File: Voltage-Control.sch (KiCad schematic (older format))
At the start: 6 parts, among them U201 MCP6002

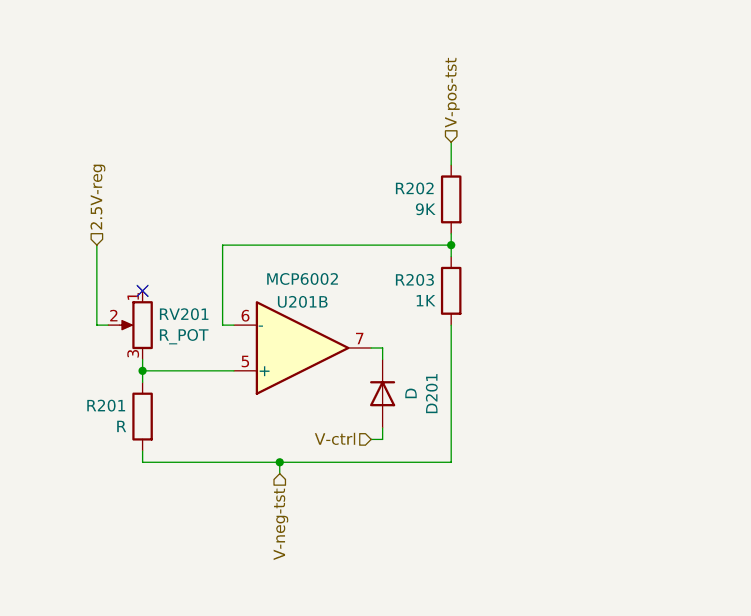
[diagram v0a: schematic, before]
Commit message: PCB completed with Op-Amp mounted horizontally
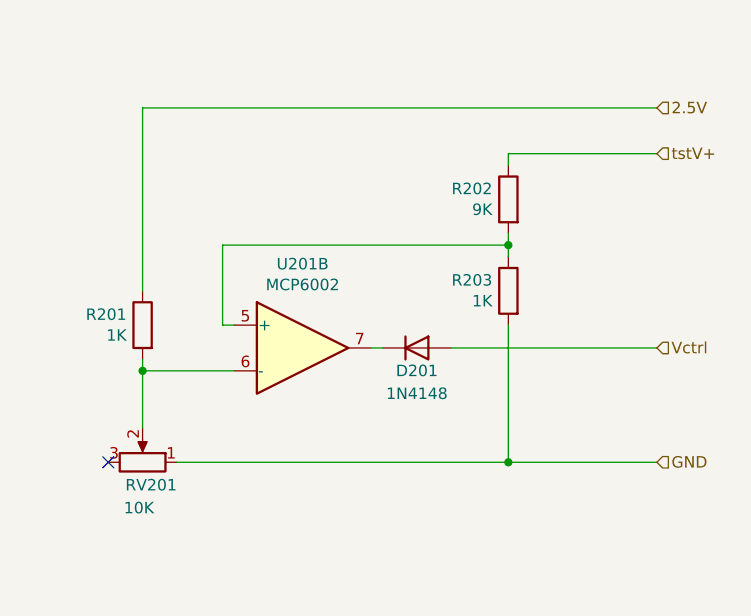
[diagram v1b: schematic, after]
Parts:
- D201: value D -> 1N4148; footprint Diode_SMD:D_SMA_Handsoldering -> Diode_SMD:D_SOD-123
- R201: value R -> 1K
- RV201: value R_POT -> 10K; footprint Potentiometer_THT:Potentiometer_Bourns_3266Y_Vertical -> f:POT_TTElect_P160KN; MPN (none) -> P160KN-0QD15B10K
- U201: footprint Package_SO:SOIC-8_3.9x4.9mm_P1.27mm -> (none)
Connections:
- net at R202.2, R203.1: now also U201.5 (+); no longer U201.6 (-)
- net GND: now reaches RV201.1
- net GND: now also R203.2
- net 2.5V-reg: no longer names the net of RV201.2
- net 2.5V-reg: now also R201.2, U201.6 (-)
- net V-ctrl renamed Vctrl
- removed net V-neg-tst: R201.2, R203.2
- net V-pos-tst renamed tstV+
- new net 2.5V: R201.1
- now unconnected: RV201.3
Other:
- moved on the sheet: D201, R201, R202, R203, RV201
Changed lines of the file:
@@
 L Device:D D?
 U 1 1 6016A51E
-P 5800 3450
+P 5950 3250
 AR Path="/6016A51E" Ref="D?"  Part="1"
 AR Path="/601B79A0/6016A51E" Ref="D201"  Part="1"
-F 0 "D201" H 5800 3667 50  0000 C CNN
-F 1 "D" H 5800 3576 50  0000 C CNN
-F 2 "Diode_SMD:D_SMA_Handsoldering" H 5800 3450 50  0001 C CNN
-F 3 "~" H 5800 3450 50  0001 C CNN
-	1    5800 3450
-	0    1    1    0
+F 0 "D201" H 5950 3150 50  0000 C CNN
+F 1 "1N4148" H 5950 3050 50  0000 C CNN
+F 2 "Diode_SMD:D_SOD-123" H 5950 3250 50  0001 C CNN
+F 3 "~" H 5950 3250 50  0001 C CNN
+	1    5950 3250
+	1    0    0    -1
 $EndComp
 $Comp
 L Device:R_POT RV?
 U 1 1 6016A525
-P 4750 3150
+P 4750 3750
 AR Path="/6016A525" Ref="RV?"  Part="1"
 AR Path="/601B79A0/6016A525" Ref="RV201"  Part="1"
-F 0 "RV201" H 4681 3196 50  0000 R CNN
-F 1 "R_POT" H 4681 3105 50  0000 R CNN
-F 2 "Potentiometer_THT:Potentiometer_Bourns_3266Y_Vertical" H 4750 3150 50  0001 C CNN
+F 0 "RV201" V 4650 3900 50  0000 R CNN
+F 1 "10K" V 4550 3800 50  0000 R CNN
+F 2 "f:POT_TTElect_P160KN" H 4750 3750 50  0001 C CNN
+F 3 "https://www.ttelectronics.com/TTElectronics/media/ProductFiles/Potentiometers/Datasheets/P160.pdf" H 4750 3750 50  0001 C CNN
+F 4 "P160KN-0QD15B10K" H 4750 3750 50  0001 C CNN "MPN"
+	1    4750 3750
+	0    1    -1   0
+$EndComp
+$Comp
+L Device:R R?
+U 1 1 6016A52B
+P 4750 3150
+AR Path="/6016A52B" Ref="R?"  Part="1"
+AR Path="/601B79A0/6016A52B" Ref="R201"  Part="1"
+F 0 "R201" H 4820 3196 50  0000 L CNN
+F 1 "1K" H 4820 3105 50  0000 L CNN
+F 2 "Resistor_SMD:R_0805_2012Metric_Pad1.20x1.40mm_HandSolder" V 4680 3150 50  0001 C CNN
 F 3 "~" H 4750 3150 50  0001 C CNN
 	1    4750 3150
 	-1   0    0    -1
 $EndComp
-$Comp
-L Device:R R?
-U 1 1 6016A52B
-P 4750 3550
-AR Path="/6016A52B" Ref="R?"  Part="1"
-AR Path="/601B79A0/6016A52B" Ref="R201"  Part="1"
-F 0 "R201" H 4820 3596 50  0000 L CNN
-F 1 "R" H 4820 3505 50  0000 L CNN
-F 2 "Resistor_SMD:R_0805_2012Metric_Pad1.20x1.40mm_HandSolder" V 4680 3550 50  0001 C CNN
-F 3 "~" H 4750 3550 50  0001 C CNN
-	1    4750 3550
-	-1   0    0    -1
-$EndComp
-Wire Wire Line
-	4750 3700 4750 3750
 Wire Wire Line
 	5100 3150 5100 2800
@@
 L Device:R R?
 U 1 1 6016A53B
-P 6100 3000
+P 6350 3000
 AR Path="/6016A53B" Ref="R?"  Part="1"
 AR Path="/601B79A0/6016A53B" Ref="R203"  Part="1"
-F 0 "R203" H 6170 3046 50  0000 L CNN
-F 1 "1K" H 6170 2955 50  0000 L CNN
-F 2 "Resistor_SMD:R_0805_2012Metric_Pad1.20x1.40mm_HandSolder" V 6030 3000 50  0001 C CNN
-F 3 "~" H 6100 3000 50  0001 C CNN
-	1    6100 3000
+F 0 "R203" H 6420 3046 50  0000 L CNN
+F 1 "1K" H 6420 2955 50  0000 L CNN
+F 2 "Resistor_SMD:R_0805_2012Metric_Pad1.20x1.40mm_HandSolder" V 6280 3000 50  0001 C CNN
+F 3 "~" H 6350 3000 50  0001 C CNN
+	1    6350 3000
 	-1   0    0    -1
 $EndComp
@@
 L Device:R R?
 U 1 1 6016A541
-P 6100 2600
+P 6350 2600
 AR Path="/6016A541" Ref="R?"  Part="1"
 AR Path="/601B79A0/6016A541" Ref="R202"  Part="1"
-F 0 "R202" H 6170 2646 50  0000 L CNN
-F 1 "9K" H 6170 2555 50  0000 L CNN
-F 2 "Resistor_SMD:R_0805_2012Metric_Pad1.20x1.40mm_HandSolder" V 6030 2600 50  0001 C CNN
-F 3 "~" H 6100 2600 50  0001 C CNN
-	1    6100 2600
+F 0 "R202" H 6420 2646 50  0000 L CNN
+F 1 "9K" H 6420 2555 50  0000 L CNN
+F 2 "Resistor_SMD:R_0805_2012Metric_Pad1.20x1.40mm_HandSolder" V 6280 2600 50  0001 C CNN
+F 3 "~" H 6350 2600 50  0001 C CNN
+	1    6350 2600
 	-1   0    0    -1
 $EndComp
 Wire Wire Line
-	6100 2750 6100 2800
+	6350 2750 6350 2800
 Wire Wire Line
-	6100 2800 5100 2800
-Connection ~ 6100 2800
+	6350 2800 5100 2800
+Connection ~ 6350 2800
 Wire Wire Line
-	6100 2800 6100 2850
-Text HLabel 6100 2350 1    50   Input ~ 0
-V-pos-tst
+	6350 2800 6350 2850
+Text HLabel 7000 2400 2    50   Input ~ 0
+tstV+
 Wire Wire Line
-	4600 3150 4550 3150
-Wire Wire Line
-	4550 3150 4550 2800
-Wire Wire Line
-	5750 3250 5800 3250
-Wire Wire Line
-	5800 3250 5800 3300
-Wire Wire Line
-	4750 3750 5350 3750
-Wire Wire Line
-	6100 3750 6100 3150
-Wire Wire Line
-	5350 3800 5350 3750
-Connection ~ 5350 3750
-Wire Wire Line
-	5350 3750 6100 3750
-NoConn ~ 4750 3000
-Text HLabel 5750 3650 0    50   Input ~ 0
-V-ctrl
-Wire Wire Line
-	5750 3650 5800 3650
-Wire Wire Line
-	5800 3650 5800 3600
-Wire Wire Line
-	6100 2350 6100 2450
-Text HLabel 4550 2800 1    50   Input ~ 0
-2.5V-reg
-Text HLabel 5350 3800 3    50   Input ~ 0
-V-neg-tst
-Wire Wire Line
-	4750 3300 4750 3350
-$Comp
-L Amplifier_Operational:MCP6002-xSN U?
-U 2 1 6016A517
-P 5450 3250
-AR Path="/6016A517" Ref="U?"  Part="2"
-AR Path="/601B79A0/6016A517" Ref="U201"  Part="2"
-F 0 "U201" H 5450 3050 50  0000 C CNN
-F 1 "MCP6002" H 5450 2950 50  0000 C CNN
-F 2 "Package_SO:SOIC-8_3.9x4.9mm_P1.27mm" H 5450 3250 50  0001 C CNN
-F 3 "http://ww1.microchip.com/downloads/en/DeviceDoc/21733j.pdf" H 5450 3250 50  0001 C CNN
-	2    5450 3250
-	1    0    0    1
-$EndComp
+	6350 3750 6350 3150
+NoConn ~ 4600 3750
+Text HLabel 7000 3250 2    50   Input ~ 0
+Vctrl
+Text HLabel 7000 2200 2    50   Input ~ 0
+2.5V
+Text HLabel 7000 3750 2    50   Input ~ 0
+GND
 Wire Wire Line
 	5100 3150 5150 3150
@@
 Connection ~ 4750 3350
 Wire Wire Line
-	4750 3350 4750 3400
+	4750 3350 4750 3600
+Wire Wire Line
+	4750 3300 4750 3350
+Wire Wire Line
+	6350 2400 6350 2450
+Wire Wire Line
+	6350 2400 7000 2400
+Connection ~ 6350 3750
+Wire Wire Line
+	6350 3750 7000 3750
+Wire Wire Line
+	4900 3750 6350 3750
+Wire Wire Line
+	4750 2200 4750 3000
+Wire Wire Line
+	4750 2200 7000 2200
+Wire Wire Line
+	5750 3250 5800 3250
+Wire Wire Line
+	6100 3250 7000 3250
+$Comp
+L Amplifier_Operational:MCP6002-xSN U201
+U 2 1 60396245
+P 5450 3250
+F 0 "U201" H 5450 3617 50  0000 C CNN
+F 1 "MCP6002" H 5450 3526 50  0000 C CNN
+F 2 "" H 5450 3250 50  0001 C CNN
+F 3 "http://ww1.microchip.com/downloads/en/DeviceDoc/21733j.pdf" H 5450 3250 50  0001 C CNN
+	2    5450 3250
+	1    0    0    -1
+$EndComp
 $EndSCHEMATC

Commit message: Revision A as sent to OSHPark with some MPN updates due to availability
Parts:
- R201, R202, R203: footprint Resistor_SMD:R_0805_2012Metric_Pad1.20x1.40mm_HandSolder -> Resistor_SMD:R_0603_1608Metric_Pad0.98x0.95mm_HandSolder
- U201: footprint (none) -> Package_SO:SOIC-8_3.9x4.9mm_P1.27mm; MPN (none) -> MCP6002T-I/SN
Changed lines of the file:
@@
 F 0 "R201" H 4820 3196 50  0000 L CNN
 F 1 "1K" H 4820 3105 50  0000 L CNN
-F 2 "Resistor_SMD:R_0805_2012Metric_Pad1.20x1.40mm_HandSolder" V 4680 3150 50  0001 C CNN
+F 2 "Resistor_SMD:R_0603_1608Metric_Pad0.98x0.95mm_HandSolder" V 4680 3150 50  0001 C CNN
 F 3 "~" H 4750 3150 50  0001 C CNN
 	1    4750 3150
@@
 F 0 "R203" H 6420 3046 50  0000 L CNN
 F 1 "1K" H 6420 2955 50  0000 L CNN
-F 2 "Resistor_SMD:R_0805_2012Metric_Pad1.20x1.40mm_HandSolder" V 6280 3000 50  0001 C CNN
+F 2 "Resistor_SMD:R_0603_1608Metric_Pad0.98x0.95mm_HandSolder" V 6280 3000 50  0001 C CNN
 F 3 "~" H 6350 3000 50  0001 C CNN
 	1    6350 3000
@@
 F 0 "R202" H 6420 2646 50  0000 L CNN
 F 1 "9K" H 6420 2555 50  0000 L CNN
-F 2 "Resistor_SMD:R_0805_2012Metric_Pad1.20x1.40mm_HandSolder" V 6280 2600 50  0001 C CNN
+F 2 "Resistor_SMD:R_0603_1608Metric_Pad0.98x0.95mm_HandSolder" V 6280 2600 50  0001 C CNN
 F 3 "~" H 6350 2600 50  0001 C CNN
 	1    6350 2600
@@
 F 0 "U201" H 5450 3617 50  0000 C CNN
 F 1 "MCP6002" H 5450 3526 50  0000 C CNN
-F 2 "" H 5450 3250 50  0001 C CNN
+F 2 "Package_SO:SOIC-8_3.9x4.9mm_P1.27mm" H 5450 3250 50  0001 C CNN
 F 3 "http://ww1.microchip.com/downloads/en/DeviceDoc/21733j.pdf" H 5450 3250 50  0001 C CNN
+F 4 "MCP6002T-I/SN" H 5450 3250 50  0001 C CNN "MPN"
 	2    5450 3250
 	1    0    0    -1

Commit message: Revision 1 release
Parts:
- R202: value 9K -> 9.1K
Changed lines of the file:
@@
 AR Path="/601B79A0/6016A541" Ref="R202"  Part="1"
 F 0 "R202" H 6420 2646 50  0000 L CNN
-F 1 "9K" H 6420 2555 50  0000 L CNN
+F 1 "9.1K" H 6420 2555 50  0000 L CNN
 F 2 "Resistor_SMD:R_0603_1608Metric_Pad0.98x0.95mm_HandSolder" V 6280 2600 50  0001 C CNN
 F 3 "~" H 6350 2600 50  0001 C CNN

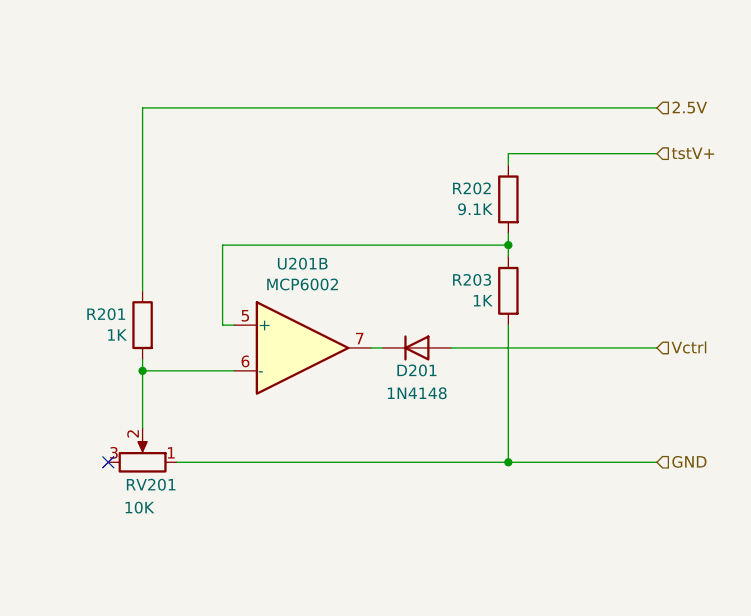
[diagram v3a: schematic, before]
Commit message: Fixed reversed Op-Amp for voltage limiting and potentiometer connections to allow for full range of the potentiometer.
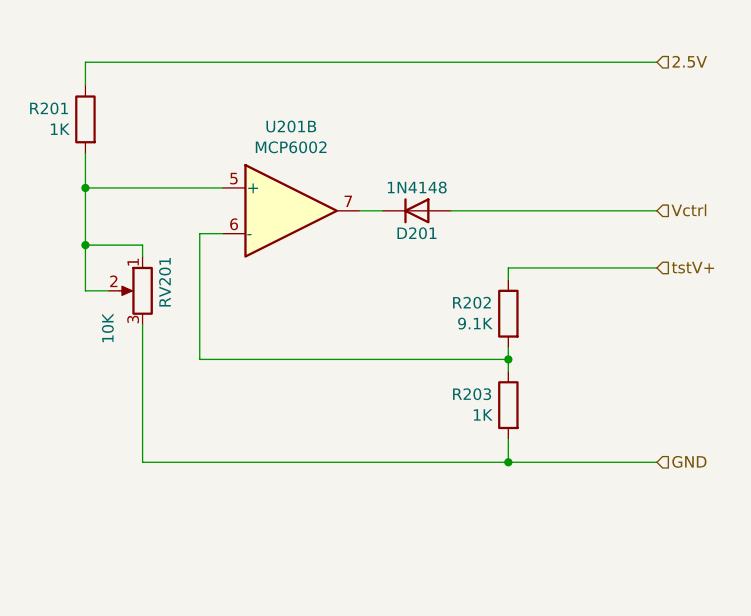
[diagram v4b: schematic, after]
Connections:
- net GND: now also RV201.3; no longer RV201.1
- net at R201.2, RV201.2: now also RV201.1, U201.5 (+); no longer U201.6 (-)
- net at R202.2, R203.1: now also U201.6 (-); no longer U201.5 (+)
- no-connect marks 1 -> 0
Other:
- moved on the sheet: D201, R201, R202, R203, RV201, U201B
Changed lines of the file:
@@
 L Device:D D?
 U 1 1 6016A51E
-P 5950 3250
+P 5950 2650
 AR Path="/6016A51E" Ref="D?"  Part="1"
 AR Path="/601B79A0/6016A51E" Ref="D201"  Part="1"
-F 0 "D201" H 5950 3150 50  0000 C CNN
-F 1 "1N4148" H 5950 3050 50  0000 C CNN
-F 2 "Diode_SMD:D_SOD-123" H 5950 3250 50  0001 C CNN
-F 3 "~" H 5950 3250 50  0001 C CNN
-	1    5950 3250
+F 0 "D201" H 5950 2550 50  0000 C CNN
+F 1 "1N4148" H 5950 2750 50  0000 C CNN
+F 2 "Diode_SMD:D_SOD-123" H 5950 2650 50  0001 C CNN
+F 3 "~" H 5950 2650 50  0001 C CNN
+	1    5950 2650
 	1    0    0    -1
 $EndComp
@@
 L Device:R_POT RV?
 U 1 1 6016A525
-P 4750 3750
+P 4750 3000
 AR Path="/6016A525" Ref="RV?"  Part="1"
 AR Path="/601B79A0/6016A525" Ref="RV201"  Part="1"
-F 0 "RV201" V 4650 3900 50  0000 R CNN
-F 1 "10K" V 4550 3800 50  0000 R CNN
-F 2 "f:POT_TTElect_P160KN" H 4750 3750 50  0001 C CNN
-F 3 "https://www.ttelectronics.com/TTElectronics/media/ProductFiles/Potentiometers/Datasheets/P160.pdf" H 4750 3750 50  0001 C CNN
-F 4 "P160KN-0QD15B10K" H 4750 3750 50  0001 C CNN "MPN"
-	1    4750 3750
-	0    1    -1   0
+F 0 "RV201" V 4650 3150 50  0000 R CNN
+F 1 "10K" V 4900 2900 50  0000 R CNN
+F 2 "f:POT_TTElect_P160KN" H 4750 3000 50  0001 C CNN
+F 3 "https://www.ttelectronics.com/TTElectronics/media/ProductFiles/Potentiometers/Datasheets/P160.pdf" H 4750 3000 50  0001 C CNN
+F 4 "P160KN-0QD15B10K" H 4750 3000 50  0001 C CNN "MPN"
+	1    4750 3000
+	-1   0    0    -1
 $EndComp
 $Comp
 L Device:R R?
 U 1 1 6016A52B
-P 4750 3150
+P 4500 2250
 AR Path="/6016A52B" Ref="R?"  Part="1"
 AR Path="/601B79A0/6016A52B" Ref="R201"  Part="1"
-F 0 "R201" H 4820 3196 50  0000 L CNN
-F 1 "1K" H 4820 3105 50  0000 L CNN
-F 2 "Resistor_SMD:R_0603_1608Metric_Pad0.98x0.95mm_HandSolder" V 4680 3150 50  0001 C CNN
-F 3 "~" H 4750 3150 50  0001 C CNN
-	1    4750 3150
+F 0 "R201" H 4570 2296 50  0000 L CNN
+F 1 "1K" H 4570 2205 50  0000 L CNN
+F 2 "Resistor_SMD:R_0603_1608Metric_Pad0.98x0.95mm_HandSolder" V 4430 2250 50  0001 C CNN
+F 3 "~" H 4500 2250 50  0001 C CNN
+	1    4500 2250
 	-1   0    0    -1
 $EndComp
-Wire Wire Line
-	5100 3150 5100 2800
 $Comp
 L Device:R R?
 U 1 1 6016A53B
-P 6350 3000
+P 6350 3500
 AR Path="/6016A53B" Ref="R?"  Part="1"
 AR Path="/601B79A0/6016A53B" Ref="R203"  Part="1"
-F 0 "R203" H 6420 3046 50  0000 L CNN
-F 1 "1K" H 6420 2955 50  0000 L CNN
-F 2 "Resistor_SMD:R_0603_1608Metric_Pad0.98x0.95mm_HandSolder" V 6280 3000 50  0001 C CNN
-F 3 "~" H 6350 3000 50  0001 C CNN
-	1    6350 3000
+F 0 "R203" H 6420 3546 50  0000 L CNN
+F 1 "1K" H 6420 3455 50  0000 L CNN
+F 2 "Resistor_SMD:R_0603_1608Metric_Pad0.98x0.95mm_HandSolder" V 6280 3500 50  0001 C CNN
+F 3 "~" H 6350 3500 50  0001 C CNN
+	1    6350 3500
 	-1   0    0    -1
 $EndComp
@@
 L Device:R R?
 U 1 1 6016A541
-P 6350 2600
+P 6350 3100
 AR Path="/6016A541" Ref="R?"  Part="1"
 AR Path="/601B79A0/6016A541" Ref="R202"  Part="1"
-F 0 "R202" H 6420 2646 50  0000 L CNN
-F 1 "9.1K" H 6420 2555 50  0000 L CNN
-F 2 "Resistor_SMD:R_0603_1608Metric_Pad0.98x0.95mm_HandSolder" V 6280 2600 50  0001 C CNN
-F 3 "~" H 6350 2600 50  0001 C CNN
-	1    6350 2600
+F 0 "R202" H 6420 3146 50  0000 L CNN
+F 1 "9.1K" H 6420 3055 50  0000 L CNN
+F 2 "Resistor_SMD:R_0603_1608Metric_Pad0.98x0.95mm_HandSolder" V 6280 3100 50  0001 C CNN
+F 3 "~" H 6350 3100 50  0001 C CNN
+	1    6350 3100
 	-1   0    0    -1
 $EndComp
-Wire Wire Line
-	6350 2750 6350 2800
-Wire Wire Line
-	6350 2800 5100 2800
-Connection ~ 6350 2800
-Wire Wire Line
-	6350 2800 6350 2850
-Text HLabel 7000 2400 2    50   Input ~ 0
+Text HLabel 7000 2900 2    50   Input ~ 0
 tstV+
 Wire Wire Line
-	6350 3750 6350 3150
-NoConn ~ 4600 3750
-Text HLabel 7000 3250 2    50   Input ~ 0
+	6350 3750 6350 3650
+Text HLabel 7000 2650 2    50   Input ~ 0
 Vctrl
-Text HLabel 7000 2200 2    50   Input ~ 0
+Text HLabel 7000 2000 2    50   Input ~ 0
 2.5V
 Text HLabel 7000 3750 2    50   Input ~ 0
 GND
 Wire Wire Line
-	5100 3150 5150 3150
+	6350 2900 6350 2950
 Wire Wire Line
-	4750 3350 5150 3350
-Connection ~ 4750 3350
-Wire Wire Line
-	4750 3350 4750 3600
-Wire Wire Line
-	4750 3300 4750 3350
-Wire Wire Line
-	6350 2400 6350 2450
-Wire Wire Line
-	6350 2400 7000 2400
-Connection ~ 6350 3750
+	6350 2900 7000 2900
 Wire Wire Line
 	6350 3750 7000 3750
 Wire Wire Line
-	4900 3750 6350 3750
+	4500 2000 7000 2000
 Wire Wire Line
-	4750 2200 4750 3000
+	5700 2650 5800 2650
 Wire Wire Line
-	4750 2200 7000 2200
-Wire Wire Line
-	5750 3250 5800 3250
-Wire Wire Line
-	6100 3250 7000 3250
+	6100 2650 7000 2650
 $Comp
 L Amplifier_Operational:MCP6002-xSN U201
 U 2 1 60396245
-P 5450 3250
-F 0 "U201" H 5450 3617 50  0000 C CNN
-F 1 "MCP6002" H 5450 3526 50  0000 C CNN
-F 2 "Package_SO:SOIC-8_3.9x4.9mm_P1.27mm" H 5450 3250 50  0001 C CNN
-F 3 "http://ww1.microchip.com/downloads/en/DeviceDoc/21733j.pdf" H 5450 3250 50  0001 C CNN
-F 4 "MCP6002T-I/SN" H 5450 3250 50  0001 C CNN "MPN"
-	2    5450 3250
+P 5400 2650
+F 0 "U201" H 5400 3017 50  0000 C CNN
+F 1 "MCP6002" H 5400 2926 50  0000 C CNN
+F 2 "Package_SO:SOIC-8_3.9x4.9mm_P1.27mm" H 5400 2650 50  0001 C CNN
+F 3 "http://ww1.microchip.com/downloads/en/DeviceDoc/21733j.pdf" H 5400 2650 50  0001 C CNN
+F 4 "MCP6002T-I/SN" H 5400 2650 50  0001 C CNN "MPN"
+	2    5400 2650
 	1    0    0    -1
 $EndComp
+Wire Wire Line
+	6350 3300 6350 3350
+Connection ~ 6350 3300
+Wire Wire Line
+	6350 3250 6350 3300
+Wire Wire Line
+	5000 3300 5000 2750
+Wire Wire Line
+	5000 2750 5100 2750
+Wire Wire Line
+	5000 3300 6350 3300
+Wire Wire Line
+	4500 2100 4500 2000
+Wire Wire Line
+	4750 3150 4750 3750
+Wire Wire Line
+	4750 3750 6350 3750
+Connection ~ 6350 3750
+Wire Wire Line
+	4500 2400 4500 2550
+Wire Wire Line
+	4500 3000 4600 3000
+Wire Wire Line
+	5100 2550 4500 2550
+Connection ~ 4500 2550
+Wire Wire Line
+	4500 2550 4500 2800
+Wire Wire Line
+	4750 2850 4750 2800
+Wire Wire Line
+	4750 2800 4500 2800
+Connection ~ 4500 2800
+Wire Wire Line
+	4500 2800 4500 3000
 $EndSCHEMATC
